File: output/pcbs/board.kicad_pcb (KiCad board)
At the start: 2 copper layers, 160.9 x 128.6 mm, 76 parts

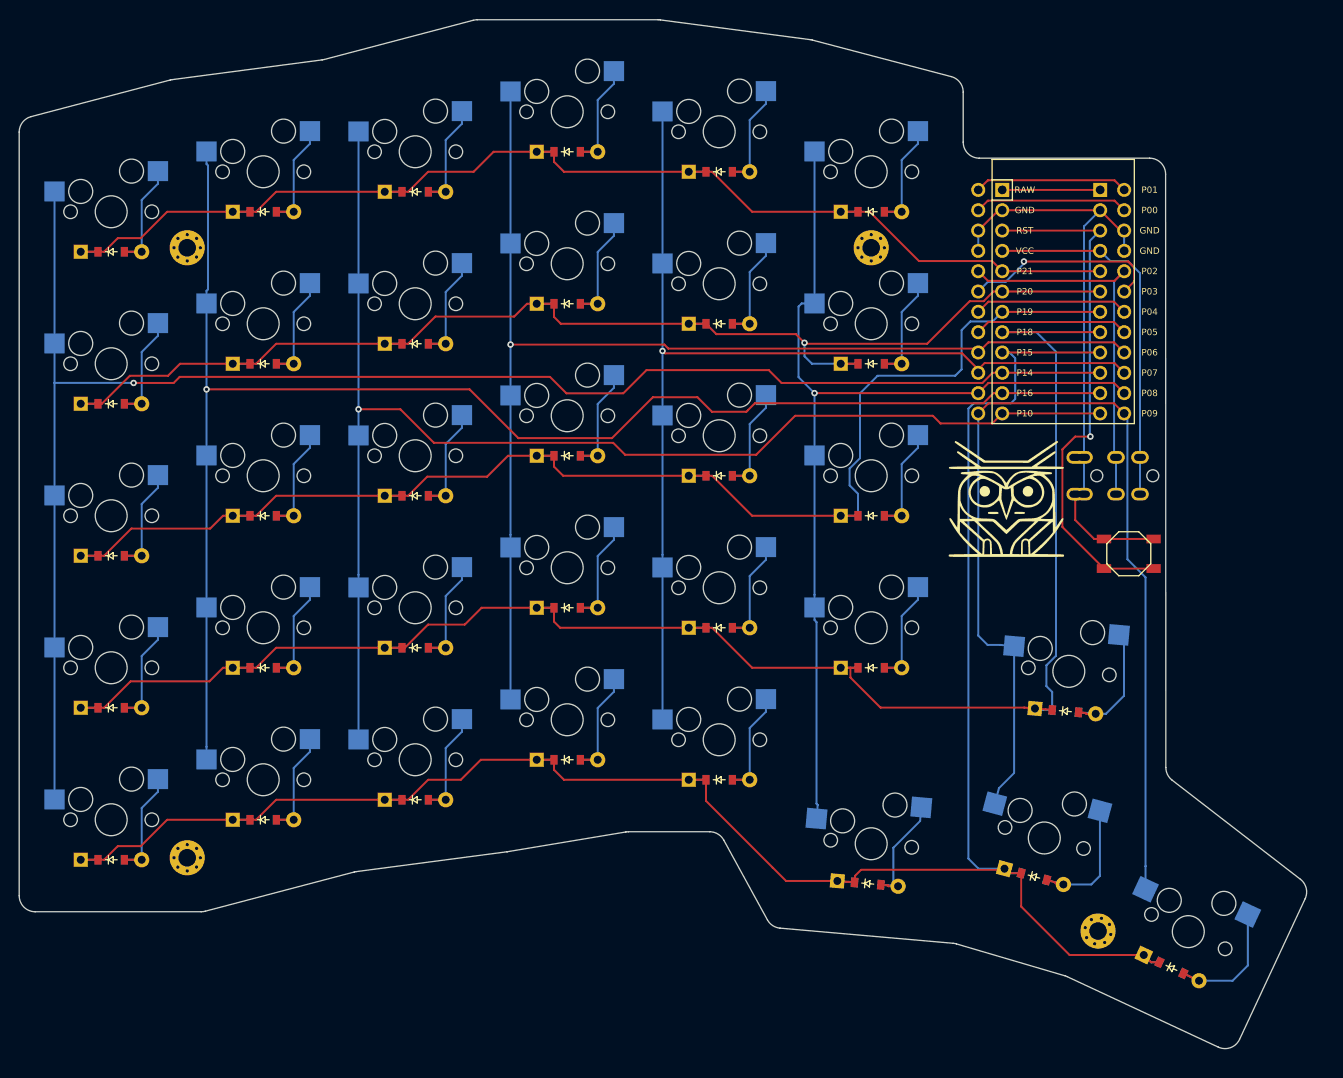
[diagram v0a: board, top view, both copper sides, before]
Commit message: ホットスワップようにフットプリントを修正
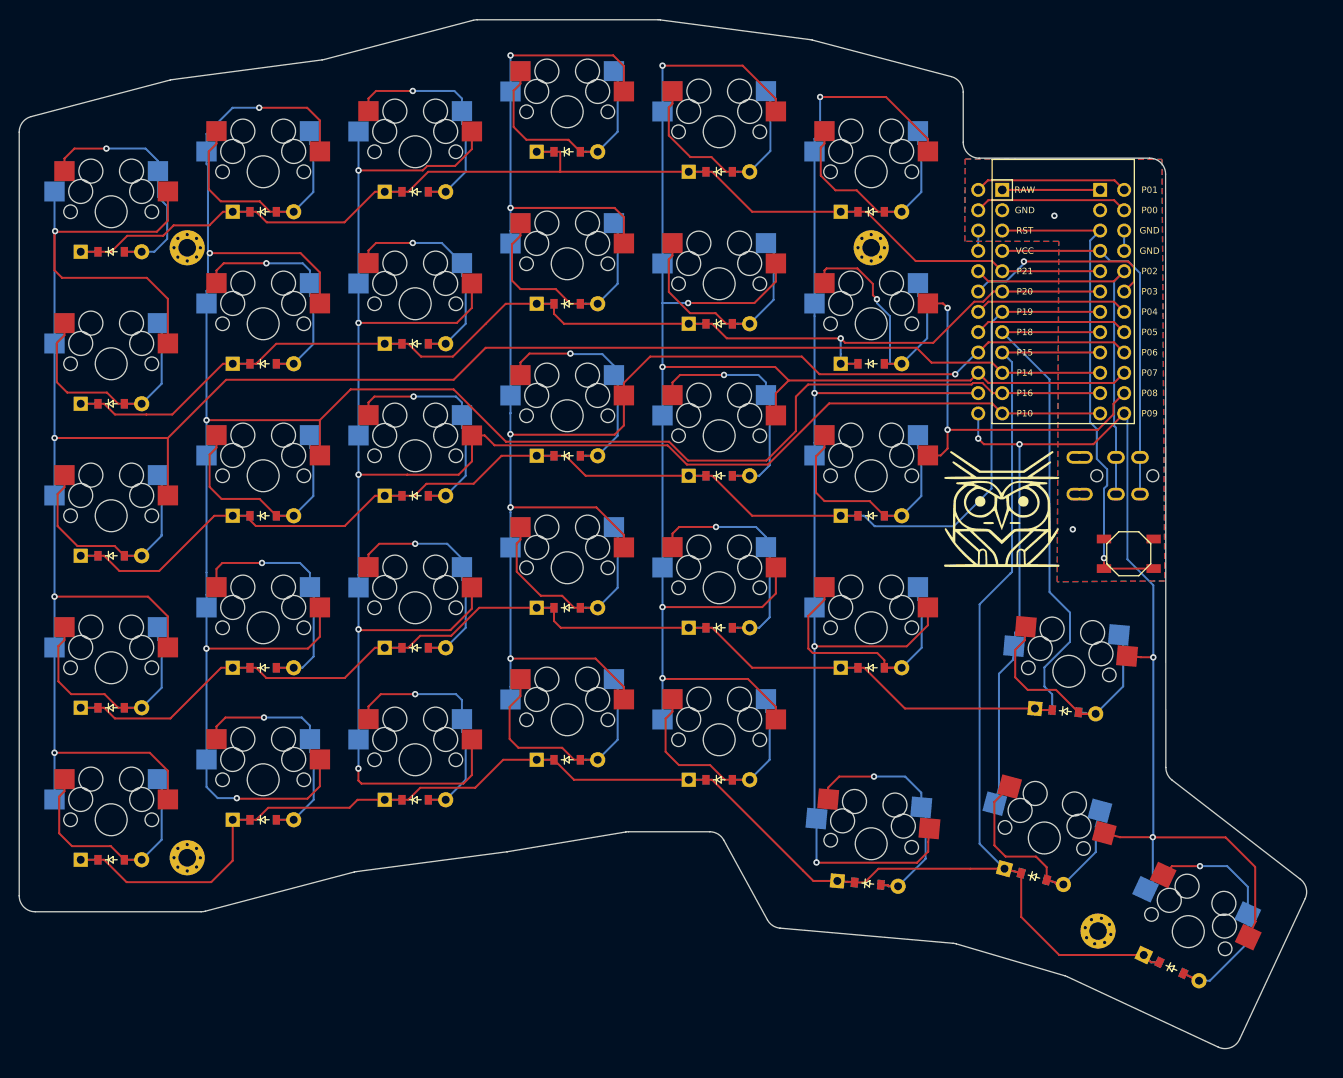
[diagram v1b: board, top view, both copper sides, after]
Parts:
- removed G*** (x2): LOGO, LOGO
- added G00: LOGO, LOGO, F.Cu at (161.3, 111.5)
- added G01: LOGO, LOGO, B.Cu at (160.6, 111.0)
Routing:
- net P8: track 125.9 -> 220.0 mm, vias 1 -> 6
- net P16: track 194.2 -> 286.2 mm, vias 1 -> 5
- net P14: track 210.3 -> 302.0 mm, vias 1 -> 4
- net P6: track 154.2 -> 237.7 mm, vias 1 -> 6
- net P10: track 174.0 -> 255.7 mm, vias 1 -> 5
- net P7: track 135.9 -> 217.0 mm, vias 1 -> 5
- net GND: track 78.0 -> 8.20 mm, vias 0 -> 2
- net P9: track 133.2 -> 163.2 mm, vias 0 -> 4
- net inner_bottom: track 15.2 -> 36.0 mm
- net inner_top: track 15.2 -> 35.6 mm, vias 0 -> 1
- net middle_mod: track 15.2 -> 33.6 mm
- net bracket_bottom: track 16.7 -> 34.7 mm
- net middle_top: track 15.2 -> 33.0 mm
- net outer_top: track 15.2 -> 33.0 mm
- net inner_home: track 15.2 -> 33.0 mm
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- added copper zone on B.Cu, net GND
- added copper zone on F.Cu, net GND

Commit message: ボタンをスルーホールに修正
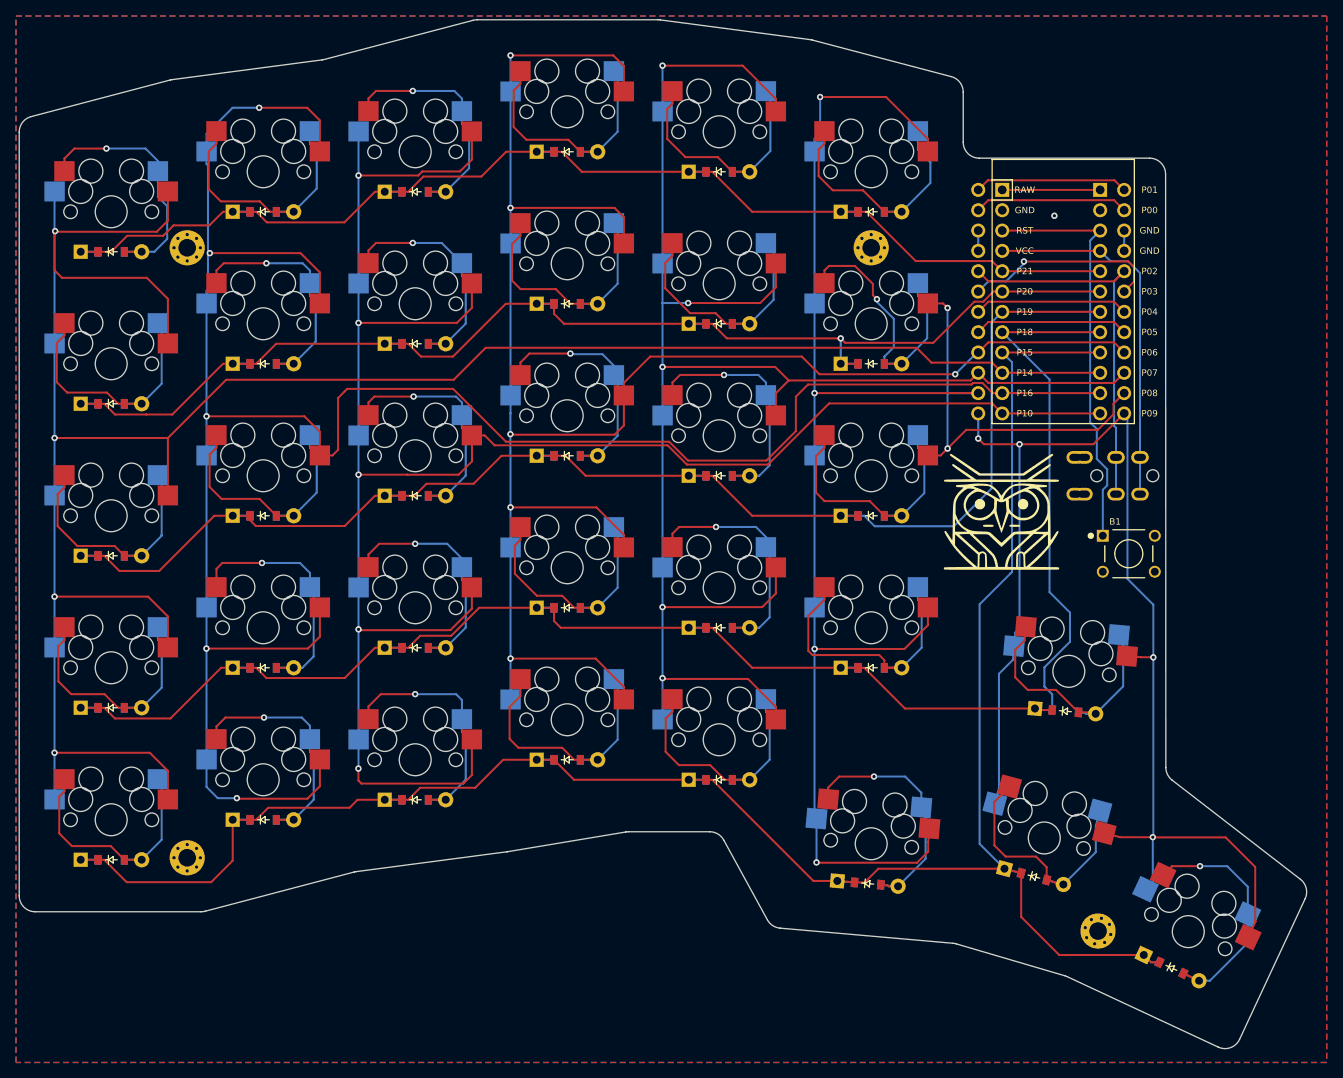
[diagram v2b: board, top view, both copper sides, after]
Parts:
- B1: value (none) -> SW_FSM8JH; footprint E73:SW_TACT_ALPS_SKQGABE010 -> SW_FSM8JH
- moved G00 0.35 mm to (161.3, 111.8)
- moved G01 0.35 mm to (160.6, 111.3)
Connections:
- B1 pad 1: GND -> RST
- B1 pad 2: RST -> GND
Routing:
- net RST: track 62.3 -> 52.0 mm, vias 1 -> 0
- net P16: track 286.2 -> 291.2 mm
- net P21: track 156.2 -> 152.8 mm
- net bracket_bottom: track 34.7 -> 32.5 mm
- net inner_num: track 31.2 -> 32.5 mm
- net P8: track 220.0 -> 221.1 mm
- net P10: track 255.7 -> 256.7 mm
- net inner_top: track 35.6 -> 36.6 mm
- net index_num: track 31.3 -> 31.8 mm
- net GND: vias 2 -> 1

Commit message: トッププレートを追加
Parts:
- removed G00, G01: LOGO, LOGO
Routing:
- net P14: track 302.0 -> 0.00 mm, vias 4 -> 0
- net P16: track 291.2 -> 0.00 mm, vias 5 -> 0
- net P15: track 257.7 -> 0.00 mm
- net P10: track 256.7 -> 0.00 mm, vias 5 -> 0
- net P6: track 237.7 -> 0.00 mm, vias 6 -> 0
- net P8: track 221.1 -> 0.00 mm, vias 6 -> 0
- net P7: track 217.4 -> 0.00 mm, vias 5 -> 0
- net P18: track 214.9 -> 0.00 mm
- net P19: track 175.4 -> 0.00 mm
- net P9: track 163.2 -> 0.00 mm, vias 4 -> 0
- net P20: track 158.8 -> 0.00 mm, vias 1 -> 0
- net P21: track 152.8 -> 0.00 mm
- net RST: track 52.0 -> 0.00 mm
- net P2: track 47.8 -> 0.00 mm
- net VCC: track 46.0 -> 0.00 mm
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- removed copper zone on B.Cu, net GND
- removed copper zone on F.Cu, net GND
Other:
- outline, holes or cut-outs redrawn
- net class Default added: clearance 0.2, trace_width 0.25, via_dia 0.8, via_drill 0.4
